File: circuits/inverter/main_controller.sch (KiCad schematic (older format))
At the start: 47 parts

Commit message: Add analog frontend, add needed libraries
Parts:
- added C? (x2): 100n, symbol Capacitor
- added C? (x3): 1µ/6.3V, symbol Capacitor
- added C?: 10n, symbol Capacitor
- added D?: LM4030, symbol LM4030
- added R?: 3k3, symbol Resistor
- added R? (x4): 220, symbol Resistor
- added R? (x2): 1k0, symbol Resistor
- added STAR?: STARPOINT, symbol STARPOINT
- added U? (x2): OPA2317, symbol DUAL_OPAMP
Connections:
- net labels added: 1V25_REF, 2V50_REF
- net labels removed: 1V20_REF
- wire segments 125 -> 170
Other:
- note added: "JTAG programmer connection"
- note added: "Option to use internal\nreference voltage source"
- moved on the sheet: C?, D?A, L?, R?

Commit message: Add more circuitry, add library content
AC current measurement
AC filter
AC switch
DC booster
DC input
Analog frontend
drivers
inverter
main controller
power supply

new components for:
standard library (e.g. relay)
AC current sensor acs722
voltage regulator LM317L

Footprints for:
AC relay
TO-220
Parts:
- Q?: value Quartz -> 10MHz
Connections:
- wire segments 170 -> 230
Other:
- note added: "actual value not critial.\nreuse a already used 0.1 % device."
- moved on the sheet: C?, D?, D?A, D?B, D?C, L?, Q?, R?, STAR?, U?A, U?B, X?

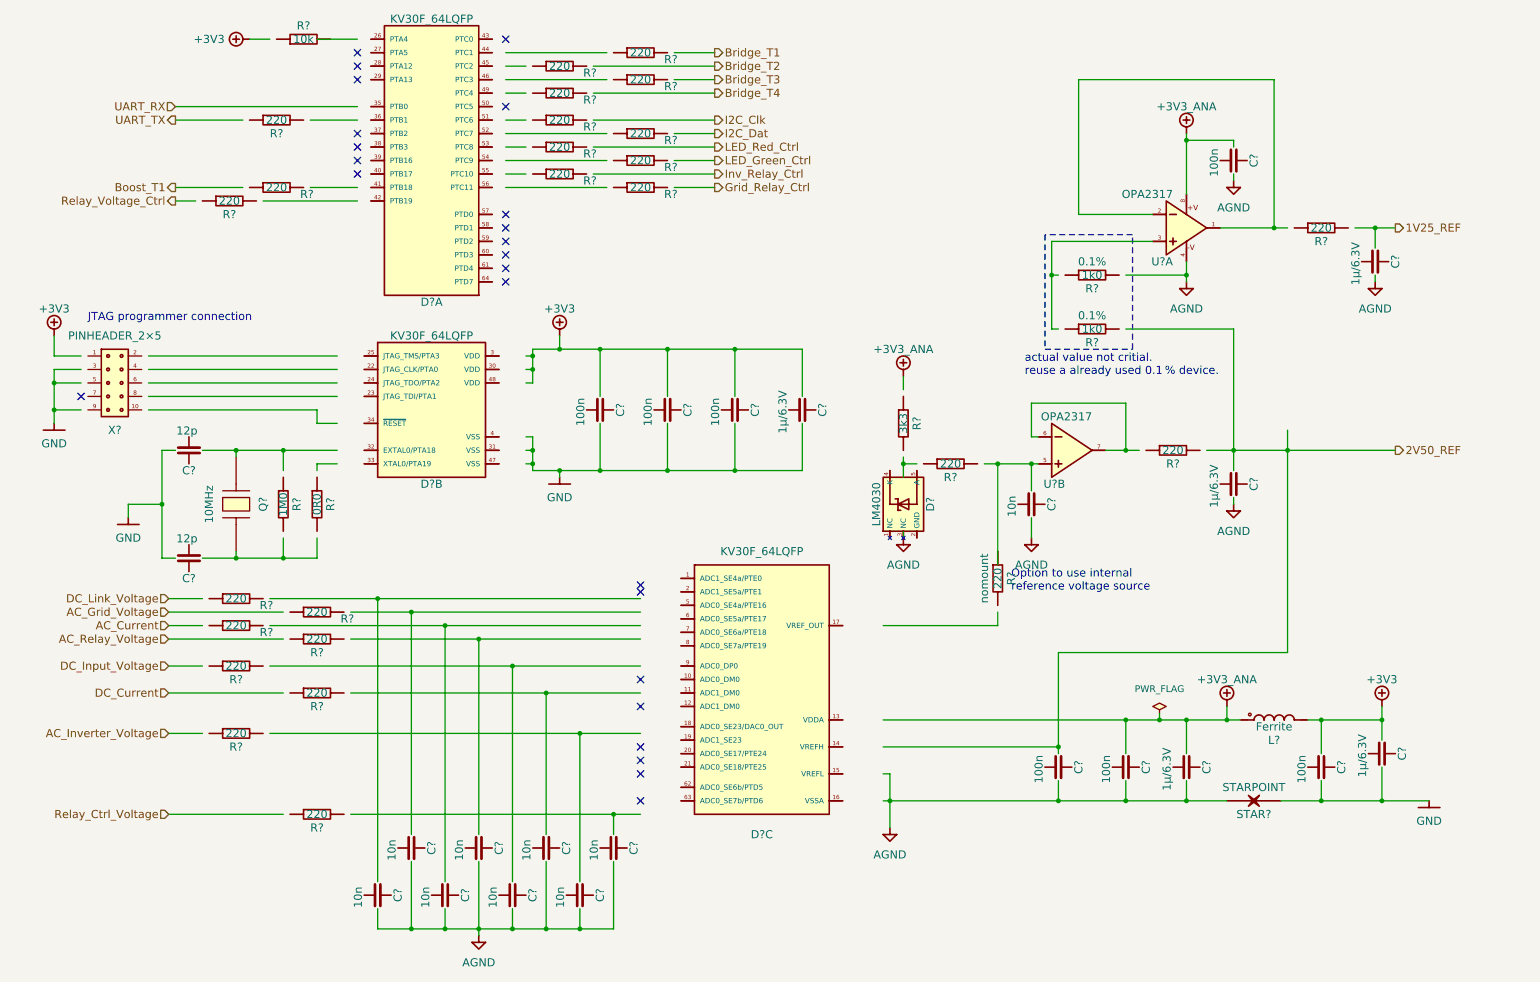
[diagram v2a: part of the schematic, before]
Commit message: Updates all schematic pages to current components
all components are replaced with the current component library parts
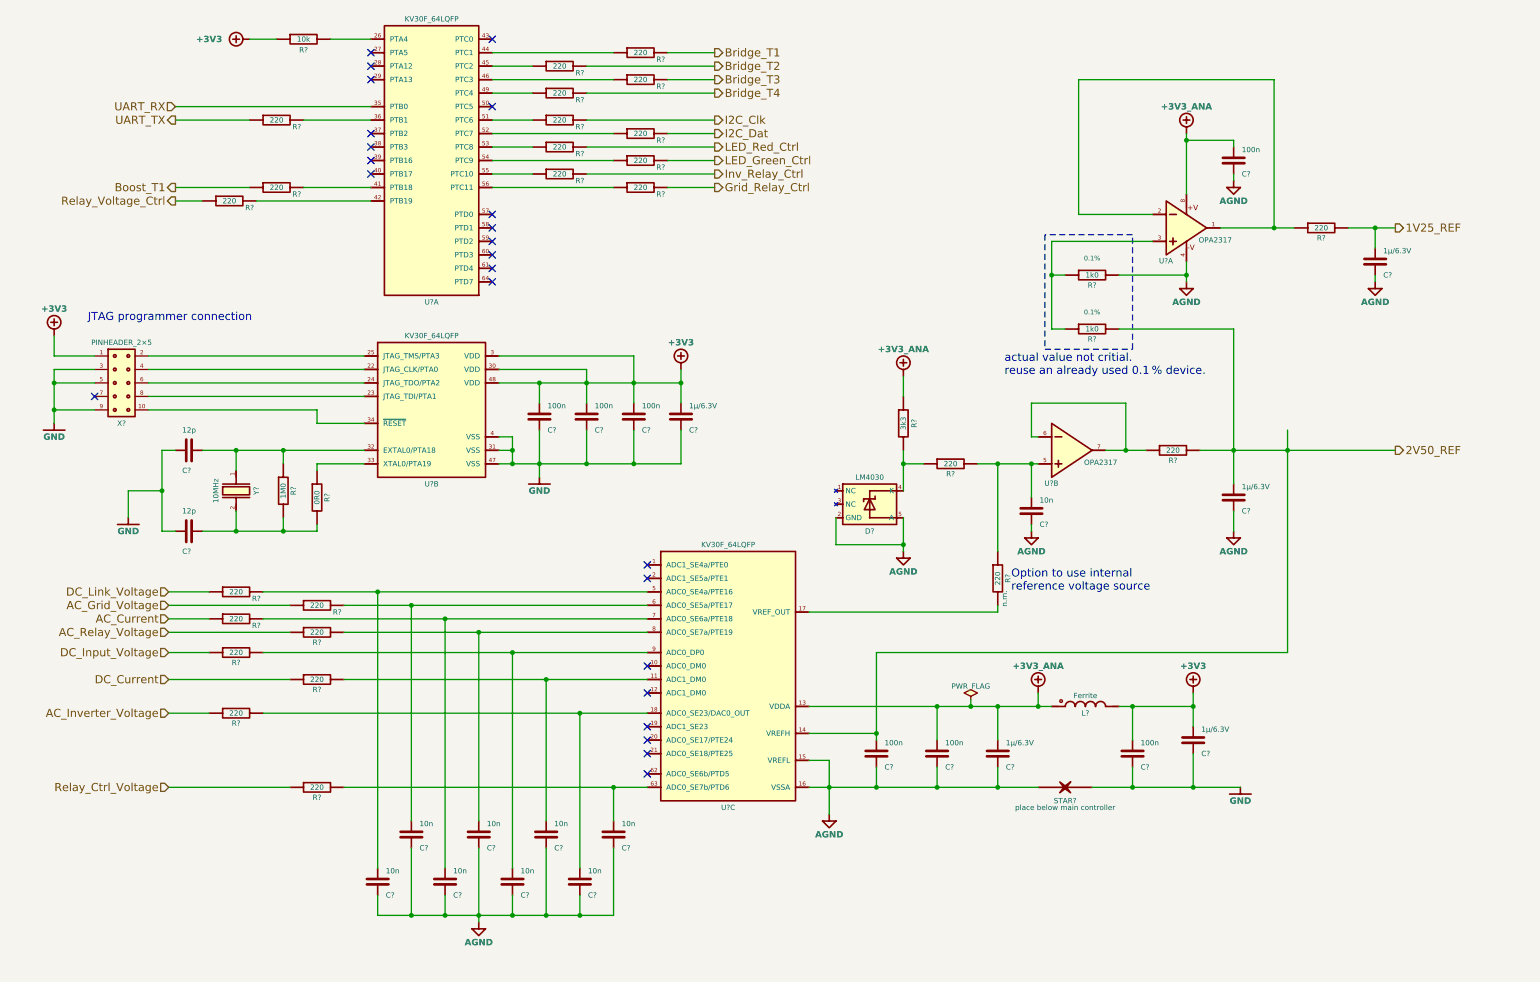
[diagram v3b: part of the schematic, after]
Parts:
- removed C? (x7): 100n, symbol Capacitor
- removed C? (x5): 1µ/6.3V, symbol Capacitor
- removed C? (x2): 12p, symbol Capacitor
- removed C? (x9): 10n, symbol Capacitor
- removed D? (x3): KV30F_64LQFP, symbol KV30F_64LQFP
- removed D?: LM4030, symbol LM4030
- removed L?: Ferrite, symbol Inductor
- removed Q?: 10MHz, symbol Quartz
- removed R?: 10k, symbol Resistor
- removed R?: 0R0, symbol Resistor
- removed R?: 1M0, symbol Resistor
- removed R? (x25): 220, symbol Resistor
- removed R?: 3k3, symbol Resistor
- removed R? (x2): 1k0, symbol Resistor
- removed STAR?: STARPOINT, symbol STARPOINT
- removed U? (x2): OPA2317, symbol DUAL_OPAMP
- removed X?: PINHEADER_2×5, symbol PINHEADER_2×5
- added C? (x9): 10n, symbol Capacitor
- added C? (x7): 100n, symbol Capacitor
- added C? (x5): 1µ/6.3V, symbol Capacitor
- added C? (x2): 12p, symbol Capacitor
- added D?: LM4030, symbol LM4030
- added L?: Ferrite, symbol Inductor
- added R?: 10k, symbol Resistor
- added R? (x25): 220, symbol Resistor
- added R?: 3k3, symbol Resistor
- added R? (x2): 1k0, symbol Resistor
- added R?: 1M0, symbol Resistor
- added R?: 0R0, symbol Resistor
- added STAR?: STARPOINT, symbol STARPOINT
- added U? (x3): KV30F_64LQFP, symbol KV30F_64LQFP
- added U? (x2): OPA2317, symbol DUAL_OPAMP
- added X?: PINHEADER_2×5, symbol PINHEADER_2×5
- added Y?: 10MHz, symbol Crystal
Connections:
- wire segments 230 -> 164
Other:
- note added: "actual value not critial.\nreuse an already used 0.1 % device."
- note removed: "actual value not critial.\nreuse a already used 0.1 % device."

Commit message: bulk-updates libraries and schematics
schematic is updated to Kicad 5.1.14
updates various sheets with new circuits
adds various component libraries
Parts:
- added C?: 100n, symbol OSSI_standard_components:Capacitor
- added R? (x2): 4k7, symbol OSSI_standard_components:Resistor
- added U?: LM75B, symbol LM75x:LM75B
- C? (x23): symbol Capacitor -> OSSI_standard_components:Capacitor
- D?: symbol LM4030 -> lm4030:LM4030
- L?: symbol Inductor -> OSSI_standard_components:Inductor
- R? (x31): symbol Resistor -> OSSI_standard_components:Resistor
- STAR?: symbol STARPOINT -> OSSI_standard_components:STARPOINT
- U? (x3): symbol KV30F_64LQFP -> kv30f:KV30F_64LQFP
- U? (x2): symbol DUAL_OPAMP -> OSSI_standard_components:DUAL_OPAMP
- X?: symbol PINHEADER_2×5 -> connectors:PINHEADER_2×5
- Y?: symbol Crystal -> OSSI_standard_components:Crystal
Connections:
- net I2C_Clk: now also R?.2, U?.2 (SCL)
- net I2C_Dat: now also R?.2, U?.1 (SDA)
- net +3V3: now reaches C?.2, C?.2, C?.2, C?.2, U?.3 (VDD), U?.30 (VDD), U?.48 (VDD)
- net +3V3: now also C?.2, C?.2, C?.2, C?.2, C?.2, L?.1, L?.2, R?.1, R?.1, U?.13 (VDDA), U?.8, X?.1, C?.2, R?.1, R?.1, U?.8 (+VS)
- net GND: now reaches C?.1, C?.1, C?.1, C?.1, U?.31 (VSS), U?.4 (VSS), U?.47 (VSS)
- net GND: now also C?.1, C?.1, C?.1, C?.1, STAR?.2, X?.3, X?.5, X?.9, C?.1, U?.4 (GND), U?.6 (A2), U?.7 (A0)
- net AGND: now reaches C?.1, C?.1, C?.1, STAR?.1, U?.15 (VREFL), U?.16 (VSSA)
- net AGND: now also C?.1, C?.1, C?.1, C?.1, C?.1, C?.1, C?.1, C?.1, C?.1, C?.1, C?.1, C?.1, D?.2 (GND), D?.5 (A), R?.2, U?.4
- no-connect marks 24 -> 25
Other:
- moved on the sheet: R?

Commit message: minor updates and cleaup
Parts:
- added R?: 220, symbol OSSI_standard_components:Resistor
- D?: footprint (none) -> OSSI_standard_footprints:SOT-23-5; Manufacturer M -> Texas Instruments
- U? (x3): footprint (none) -> OSSI_standard_footprints:LQFP-64_10x10_Pitch0.5mm
- U? (x3): footprint (none) -> OSSI_standard_footprints:SOIC8
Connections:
- net at U?.39 (PTB16): now also R?.2
- new net HISIDE_PWM_µC: R?.1
- no-connect marks 25 -> 24
